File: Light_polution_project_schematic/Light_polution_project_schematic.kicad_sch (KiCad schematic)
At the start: 23 parts, among them J1 IR_Sensor_01, J2 IR_Sensor_02, J3 IR_Sensor_03, J4 IR_Sensor_04, J5 IR_Sensor_K2063_05, J6 K2140_KIT, J7 AC_Line, M1 28BYJ-48_5V_Stepper_Motor, M2 MP2835_12V_Stepper_Motor, SW1 SW_SPST, SW2 SW_SPST, SW3 IRS201-6C, U1 DC in 7.5-45V out 5V/3A 2xUSB, U2 5V_Stepper_Motor_Driver, U3 12V_Stepper_Motor_Driver

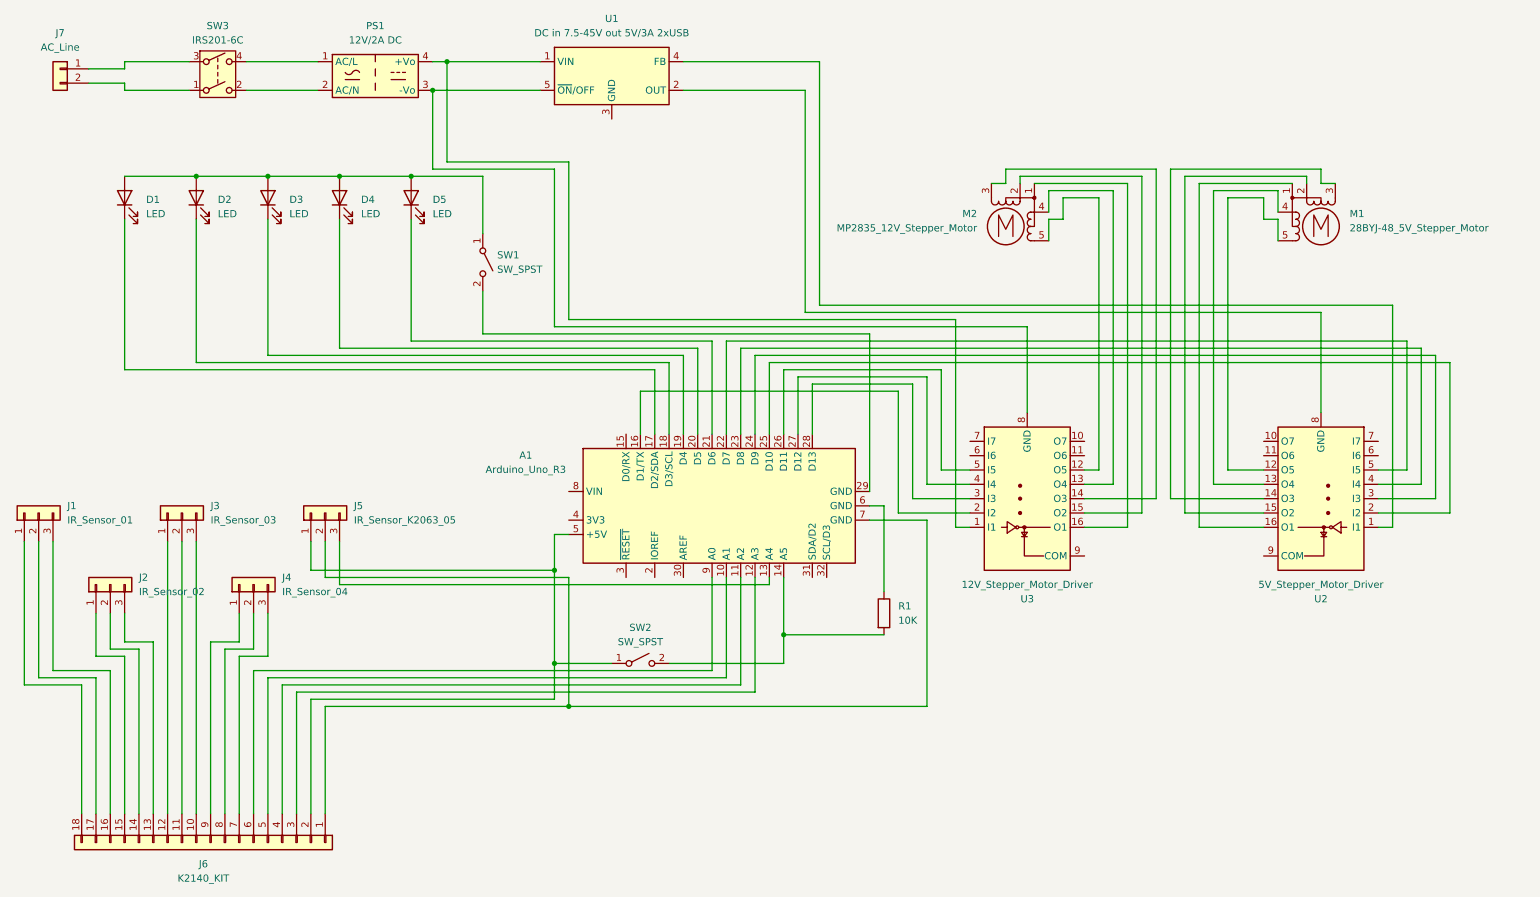
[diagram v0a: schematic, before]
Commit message: Schema updated with new motors
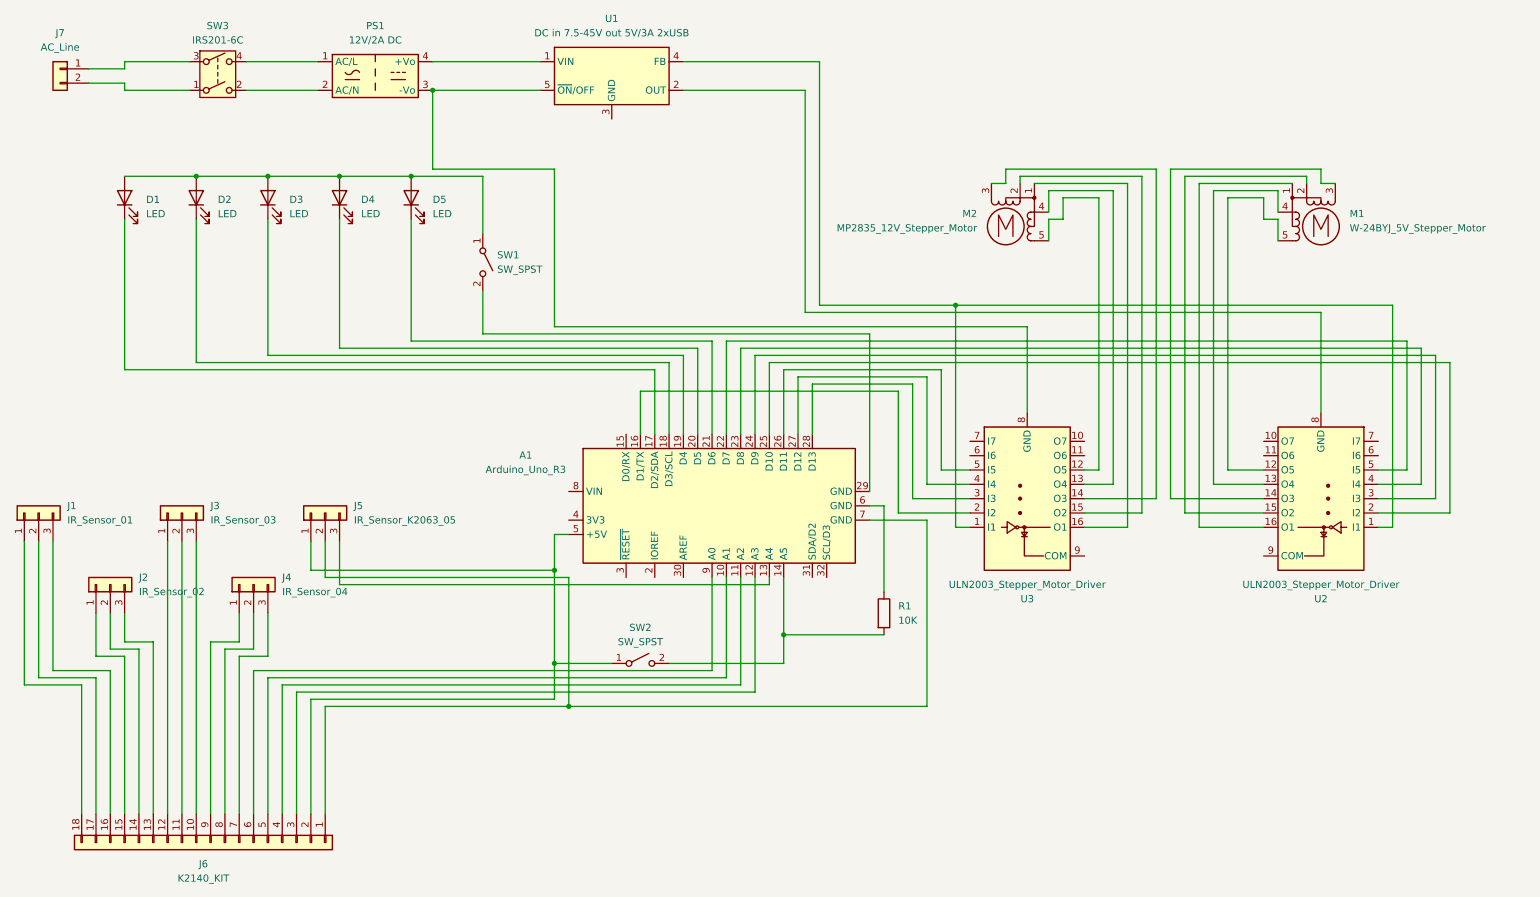
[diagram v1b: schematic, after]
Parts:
- M1: value 28BYJ-48_5V_Stepper_Motor -> W-24BYJ_5V_Stepper_Motor
- U2: value 5V_Stepper_Motor_Driver -> ULN2003_Stepper_Motor_Driver
- U3: value 12V_Stepper_Motor_Driver -> ULN2003_Stepper_Motor_Driver
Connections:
- net at U1.4 (FB), U2.1 (I1): now also U3.1 (I1)
- net at PS1.4 (+Vo), U1.1 (VIN): no longer U3.1 (I1)
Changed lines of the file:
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@@
 	)
 	(junction
+		(at 185.42 72.39)
+		(diameter 0)
+		(color 255 0 0 1)
+	)
+	(junction
 		(at 114.3 119.38)
 		(diameter 0)
@@
 		(color 0 0 0 1)
 	)
-	(junction
-		(at 95.25 29.21)
-		(diameter 0)
-		(color 255 0 0 1)
-	)
 	(wire
 		(pts
@@
 	(wire
 		(pts
-			(xy 185.42 74.93) (xy 116.84 74.93)
-		)
-		(stroke
-			(width 0)
-			(type default)
-			(color 255 0 0 1)
-		)
-	)
-	(wire
-		(pts
 			(xy 270.51 81.28) (xy 270.51 106.68)
 		)
@@
 	(wire
 		(pts
-			(xy 116.84 74.93) (xy 116.84 46.99)
-		)
-		(stroke
-			(width 0)
-			(type default)
-			(color 255 0 0 1)
-		)
-	)
-	(wire
-		(pts
 			(xy 228.6 50.8) (xy 228.6 111.76)
 		)
@@
 	(wire
 		(pts
-			(xy 116.84 46.99) (xy 95.25 46.99)
-		)
-		(stroke
-			(width 0)
-			(type default)
-			(color 255 0 0 1)
-		)
-	)
-	(wire
-		(pts
 			(xy 76.2 114.3) (xy 76.2 121.92)
 		)
@@
 	(wire
 		(pts
-			(xy 95.25 29.21) (xy 111.76 29.21)
+			(xy 92.71 29.21) (xy 111.76 29.21)
 		)
 		(stroke
@@
 	(wire
 		(pts
-			(xy 185.42 111.76) (xy 185.42 74.93)
+			(xy 185.42 72.39) (xy 185.42 111.76)
 		)
 		(stroke
@@
 	(wire
 		(pts
-			(xy 92.71 29.21) (xy 95.25 29.21)
-		)
-		(stroke
-			(width 0)
-			(type default)
-			(color 255 0 0 1)
-		)
-	)
-	(wire
-		(pts
 			(xy 240.03 57.15) (xy 242.57 57.15)
 		)
@@
 	(wire
 		(pts
+			(xy 185.42 72.39) (xy 161.29 72.39)
+		)
+		(stroke
+			(width 0)
+			(type default)
+			(color 255 0 0 1)
+		)
+	)
+	(wire
+		(pts
 			(xy 223.52 48.26) (xy 223.52 106.68)
 		)
@@
 	(wire
 		(pts
-			(xy 262.89 72.39) (xy 161.29 72.39)
+			(xy 262.89 72.39) (xy 185.42 72.39)
 		)
 		(stroke
@@
 	(wire
 		(pts
-			(xy 95.25 46.99) (xy 95.25 29.21)
-		)
-		(stroke
-			(width 0)
-			(type default)
-			(color 255 0 0 1)
-		)
-	)
-	(wire
-		(pts
 			(xy 144.78 78.74) (xy 144.78 95.25)
 		)
@@
 			)
 		)
-		(property "Value" "28BYJ-48_5V_Stepper_Motor"
+		(property "Value" "W-24BYJ_5V_Stepper_Motor"
 			(at 255.27 58.712 0)
 			(effects
@@
 			)
 		)
-		(property "Value" "5V_Stepper_Motor_Driver"
+		(property "Value" "ULN2003_Stepper_Motor_Driver"
 			(at 250.19 121.92 0)
 			(effects
@@
 			)
 		)
-		(property "Value" "12V_Stepper_Motor_Driver"
+		(property "Value" "ULN2003_Stepper_Motor_Driver"
 			(at 198.12 121.92 0)
 			(effects
